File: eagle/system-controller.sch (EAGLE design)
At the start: 225 parts, among them J1 1, Q1 MOSFET-P-N-PAIR, Q10 MOSFET-P-N-PAIR, Q11 DNP/NTR4101P, Q2 MOSFET-P-N-PAIR, Q3 DON3035L, Q4 MOSFET-P-N-PAIR, Q5 MOSFET-P-N-PAIR, Q6 MOSFET-P-N-PAIR, Q7 MOSFET-P-N-PAIR, Q8 MOSFET-P-N-PAIR, Q9 DNP/NTR4101P, U1 TPS25944LRVCRWQFN-20-3X4, U10 TPS25944LRVCRWQFN-20-3X4, U11 ACPL-M61L, U12 ACPL-M61L, U13 TPS25944LRVCRWQFN-20-3X4, U14 ACPL-M61L, U15 ACPL-M61L, U2 LP5907MFX-3.0, U3 TPS25944LRVCRWQFN-20-3X4, U4 TPS25944LRVCRWQFN-20-3X4, U5 TPS25944LRVCRWQFN-20-3X4, U6 TPS25944LRVCRWQFN-20-3X4, U7 ATMEGA128L-8A(U/N), U8 TS4100, U9 TPS25944LRVCRWQFN-20-3X4, X1 8 MHz CRYSTAL-ABRACON-ABM3-SMD

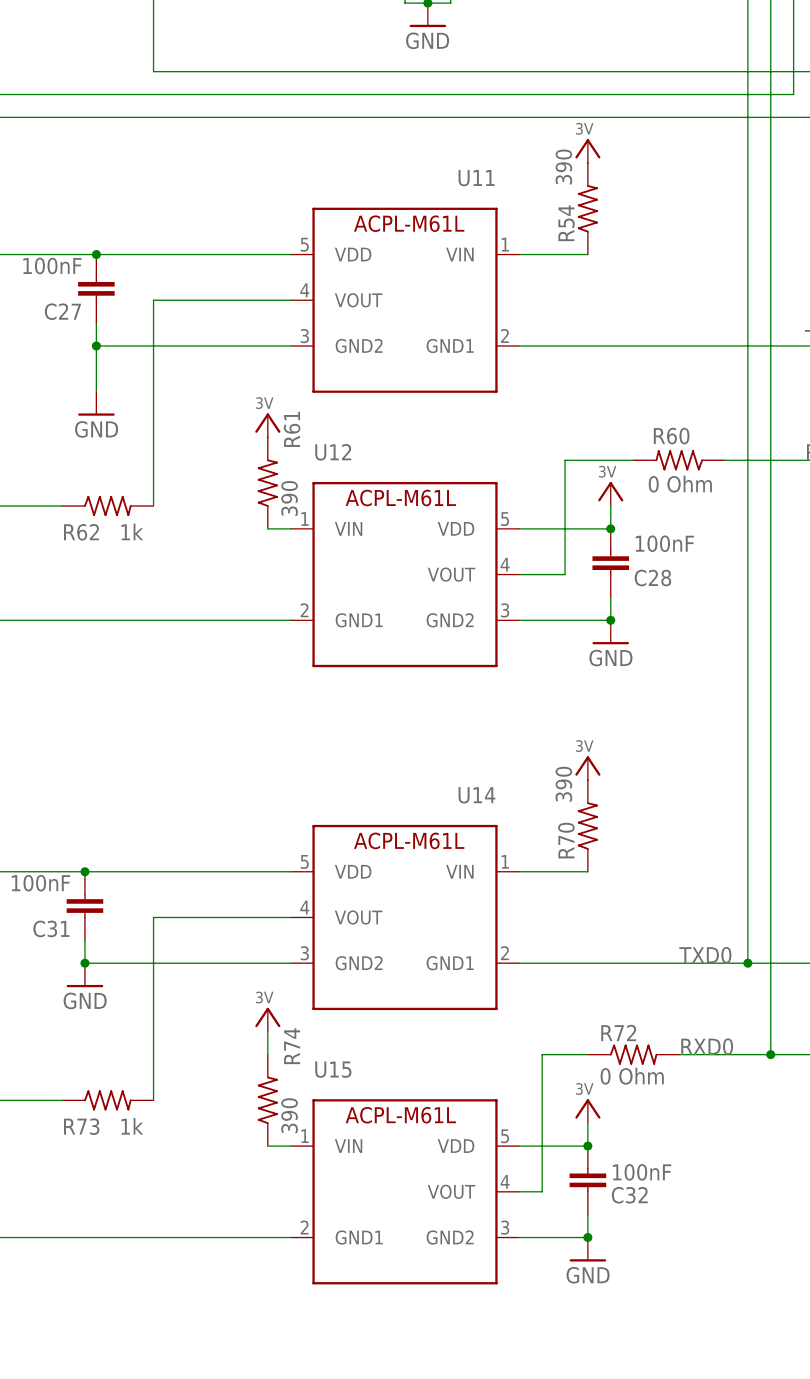
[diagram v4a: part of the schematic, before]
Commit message: Fixed opto-isolator symbol with proper labels
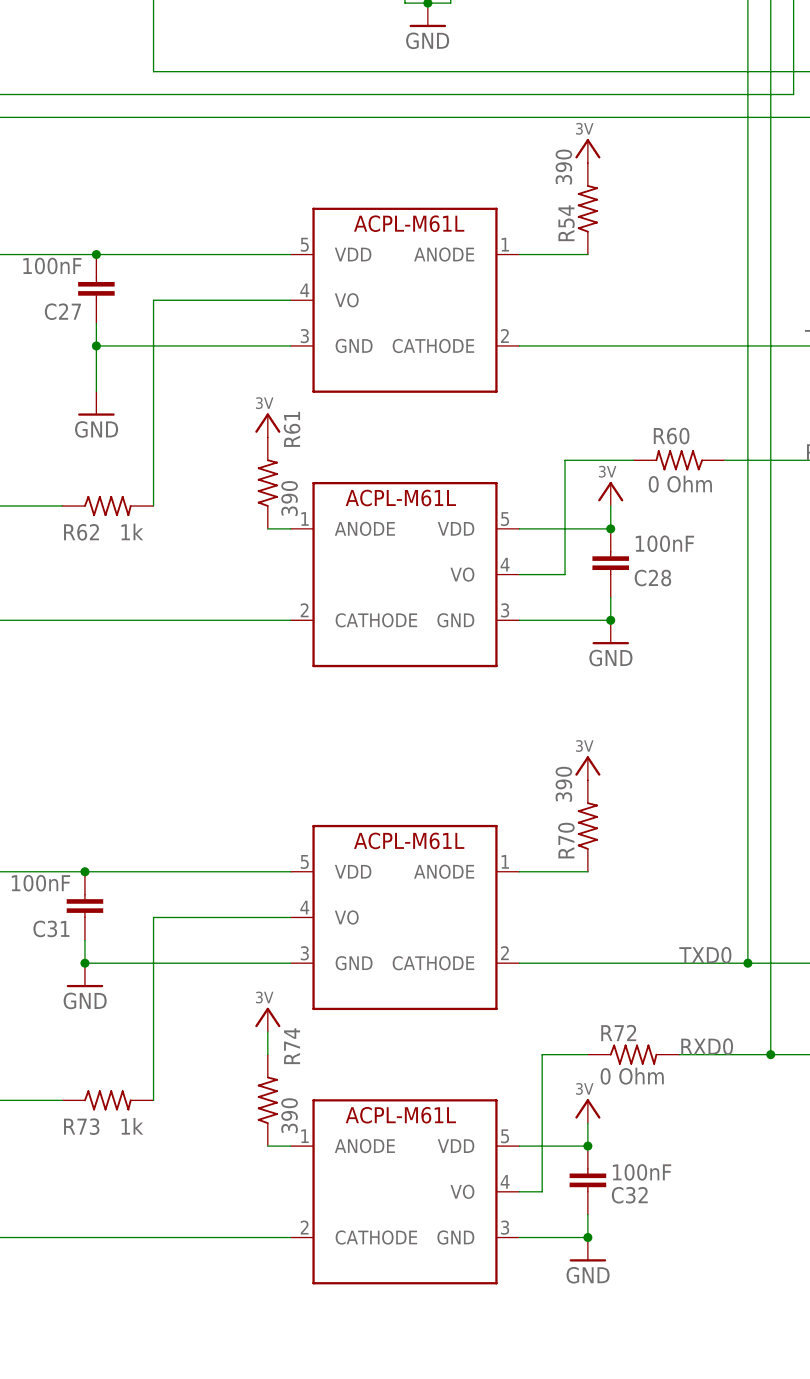
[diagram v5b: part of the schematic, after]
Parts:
- removed U11, U12, U14, U15: ACPL-M61L, v2_sync_box:ACPL-M61L
- added U$1, U$2, U$3, U$4: ACPL-M61L, system-controller:ACPL-M61L
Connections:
- net 3V: now also U$3.VDD, U$4.VDD; no longer U12.VDD, U15.VDD
- net GND: now also U$1.GND, U$2.GND, U$3.GND, U$4.GND; no longer U11.GND2, U12.GND2, U14.GND2, U15.GND2
- net N$16: now also U$2.VO; no longer U14.VOUT
- net N$18: now also U$4.VO; no longer U15.VOUT
- net N$24: now also U$3.VO; no longer U12.VOUT
- net N$4: now also U$2.ANODE; no longer U14.VIN
- net N$5: now also U$1.VO; no longer U11.VOUT
- net N$54: now also U$4.ANODE; no longer U15.VIN
- net N$58: now also U$1.ANODE; no longer U11.VIN
- net N$8: now also U$3.ANODE; no longer U12.VIN
- net TXD0: now also U$2.CATHODE; no longer U14.GND1
- net TXD1: now also U$1.CATHODE; no longer U11.GND1
- net UART_FC_TX: now also U$3.CATHODE; no longer U12.GND1
- net UART_FC_VCC: now also U$1.VDD; no longer U11.VDD
- net UART_LGR_TX: now also U$4.CATHODE; no longer U15.GND1
- net UART_LGR_VCC: now also U$2.VDD; no longer U14.VDD
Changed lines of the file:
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@@
 <?xml version="1.0" encoding="utf-8"?>
 <!DOCTYPE eagle SYSTEM "eagle.dtd">
-<eagle version="7.3.0">
+<eagle version="7.6.0">
 <drawing>
 <settings>
@@
 <attribute name="MPN" value="LP5907MFX-3.0/NOPB"/>
 </part>
-<part name="U11" library="v2_sync_box" deviceset="ACPL-M61L" device="">
-<attribute name="DIST" value="digikey"/>
-<attribute name="DPN" value="516-2169-5-ND"/>
-<attribute name="MFN" value="Broadcom"/>
-<attribute name="MPN" value="ACPL-M61L-000E"/>
-</part>
-<part name="U12" library="v2_sync_box" deviceset="ACPL-M61L" device="">
-<attribute name="DIST" value="digikey"/>
-<attribute name="DPN" value="516-2169-5-ND"/>
-<attribute name="MFN" value="Broadcom"/>
-<attribute name="MPN" value="ACPL-M61L-000E"/>
-</part>
-<part name="U14" library="v2_sync_box" deviceset="ACPL-M61L" device="">
-<attribute name="DIST" value="digikey"/>
-<attribute name="DPN" value="516-2169-5-ND"/>
-<attribute name="MFN" value="Broadcom"/>
-<attribute name="MPN" value="ACPL-M61L-000E"/>
-</part>
-<part name="U15" library="v2_sync_box" deviceset="ACPL-M61L" device="">
-<attribute name="DIST" value="digikey"/>
-<attribute name="DPN" value="516-2169-5-ND"/>
-<attribute name="MFN" value="Broadcom"/>
-<attribute name="MPN" value="ACPL-M61L-000E"/>
-</part>
 <part name="U1" library="system-controller" deviceset="TPS25944LRVCR" device="WQFN-20-3X4">
 <attribute name="DIST" value="digikey"/>
@@
 <part name="GND2" library="psas_c3_team05" deviceset="GND" device=""/>
 <part name="3V-11" library="supply-3v" deviceset="3V" device=""/>
+<part name="U$1" library="system-controller" deviceset="ACPL-M61L" device=""/>
+<part name="U$2" library="system-controller" deviceset="ACPL-M61L" device=""/>
+<part name="U$3" library="system-controller" deviceset="ACPL-M61L" device=""/>
+<part name="U$4" library="system-controller" deviceset="ACPL-M61L" device=""/>
 </parts>
 <sheets>
@@
 <attribute name="MPN" x="167.64" y="387.35" size="1.778" layer="96" display="off"/>
 </instance>
-<instance part="U11" gate="G$1" x="175.26" y="119.38" rot="MR0">
-<attribute name="DIST" x="175.26" y="119.38" size="1.778" layer="96" rot="MR0" display="off"/>
-<attribute name="DPN" x="175.26" y="119.38" size="1.778" layer="96" rot="MR0" display="off"/>
-<attribute name="MFN" x="175.26" y="119.38" size="1.778" layer="96" rot="MR0" display="off"/>
-<attribute name="MPN" x="175.26" y="119.38" size="1.778" layer="96" rot="MR0" display="off"/>
-</instance>
-<instance part="U12" gate="G$1" x="175.26" y="88.9">
-<attribute name="DIST" x="175.26" y="88.9" size="1.778" layer="96" display="off"/>
-<attribute name="MPN" x="175.26" y="88.9" size="1.778" layer="96" display="off"/>
-<attribute name="MFN" x="175.26" y="88.9" size="1.778" layer="96" display="off"/>
-<attribute name="DPN" x="175.26" y="88.9" size="1.778" layer="96" display="off"/>
-</instance>
-<instance part="U14" gate="G$1" x="175.26" y="50.8" rot="MR0">
-<attribute name="DIST" x="175.26" y="50.8" size="1.778" layer="96" rot="MR0" display="off"/>
-<attribute name="MPN" x="175.26" y="50.8" size="1.778" layer="96" rot="MR0" display="off"/>
-<attribute name="MFN" x="175.26" y="50.8" size="1.778" layer="96" rot="MR0" display="off"/>
-<attribute name="DPN" x="175.26" y="50.8" size="1.778" layer="96" rot="MR0" display="off"/>
-</instance>
-<instance part="U15" gate="G$1" x="175.26" y="20.32">
-<attribute name="DIST" x="175.26" y="20.32" size="1.778" layer="96" display="off"/>
-<attribute name="MPN" x="175.26" y="20.32" size="1.778" layer="96" display="off"/>
-<attribute name="MFN" x="175.26" y="20.32" size="1.778" layer="96" display="off"/>
-<attribute name="DPN" x="175.26" y="20.32" size="1.778" layer="96" display="off"/>
-</instance>
 <instance part="U1" gate="G$1" x="434.34" y="408.94">
 <attribute name="MPN" x="434.34" y="408.94" size="1.778" layer="96" display="off"/>
@@
 <instance part="GND2" gate="1" x="210.82" y="370.84"/>
 <instance part="3V-11" gate="G$1" x="210.82" y="393.7"/>
+<instance part="U$1" gate="G$1" x="175.26" y="119.38" rot="MR0"/>
+<instance part="U$2" gate="G$1" x="175.26" y="50.8" rot="MR0"/>
+<instance part="U$3" gate="G$1" x="175.26" y="88.9"/>
+<instance part="U$4" gate="G$1" x="175.26" y="20.32"/>
 </instances>
 <busses>
@@
 <segment>
 <wire x1="109.22" y1="83.82" x2="162.56" y2="83.82" width="0.1524" layer="91"/>
-<pinref part="U12" gate="G$1" pin="GND1"/>
 <label x="111.76" y="83.82" size="1.778" layer="95"/>
+<pinref part="U$3" gate="G$1" pin="CATHODE"/>
 </segment>
 </net>
@@
 <pinref part="LED11" gate="LED" pin="K"/>
 <wire x1="228.6" y1="45.72" x2="228.6" y2="48.26" width="0.1524" layer="91"/>
-<pinref part="U14" gate="G$1" pin="GND1"/>
+<pinref part="U$2" gate="G$1" pin="CATHODE"/>
 </segment>
 </net>
@@
 <wire x1="256.54" y1="114.3" x2="256.54" y2="121.92" width="0.1524" layer="91"/>
 <junction x="228.6" y="114.3"/>
-<pinref part="U11" gate="G$1" pin="GND1"/>
+<pinref part="U$1" gate="G$1" pin="CATHODE"/>
 </segment>
 </net>
@@
 <wire x1="147.32" y1="119.38" x2="147.32" y2="96.52" width="0.1524" layer="91"/>
 <pinref part="R62" gate="R" pin="2"/>
-<pinref part="U11" gate="G$1" pin="VOUT"/>
+<pinref part="U$1" gate="G$1" pin="VO"/>
 </segment>
 </net>
@@
 <wire x1="147.32" y1="50.8" x2="147.32" y2="30.48" width="0.1524" layer="91"/>
 <pinref part="R73" gate="R" pin="2"/>
-<pinref part="U14" gate="G$1" pin="VOUT"/>
+<pinref part="U$2" gate="G$1" pin="VO"/>
 </segment>
 </net>
@@
 <wire x1="187.96" y1="20.32" x2="190.5" y2="20.32" width="0.1524" layer="91"/>
 <wire x1="190.5" y1="20.32" x2="190.5" y2="35.56" width="0.1524" layer="91"/>
-<pinref part="U15" gate="G$1" pin="VOUT"/>
+<pinref part="U$4" gate="G$1" pin="VO"/>
 </segment>
 </net>
@@
 <segment>
 <wire x1="106.68" y1="15.24" x2="162.56" y2="15.24" width="0.1524" layer="91"/>
-<pinref part="U15" gate="G$1" pin="GND1"/>
 <label x="109.22" y="15.24" size="1.778" layer="95"/>
+<pinref part="U$4" gate="G$1" pin="CATHODE"/>
 </segment>
 </net>
@@
 <wire x1="193.04" y1="88.9" x2="187.96" y2="88.9" width="0.1524" layer="91"/>
 <pinref part="R60" gate="R" pin="2"/>
-<pinref part="U12" gate="G$1" pin="VOUT"/>
+<pinref part="U$3" gate="G$1" pin="VO"/>
 </segment>
 </net>
@@
 <pinref part="C31" gate="CE" pin="2"/>
 <junction x="139.7" y="55.88"/>
-<pinref part="U14" gate="G$1" pin="VDD"/>
+<pinref part="U$2" gate="G$1" pin="VDD"/>
 </segment>
 <segment>
@@
 <pinref part="C27" gate="CE" pin="2"/>
 <junction x="140.97" y="124.46"/>
-<pinref part="U11" gate="G$1" pin="VDD"/>
+<pinref part="U$1" gate="G$1" pin="VDD"/>
 </segment>
 <segment>
@@
 <wire x1="187.96" y1="93.98" x2="198.12" y2="93.98" width="0.1524" layer="91"/>
 <junction x="198.12" y="93.98"/>
-<pinref part="U12" gate="G$1" pin="VDD"/>
+<pinref part="U$3" gate="G$1" pin="VDD"/>
 </segment>
 <segment>
@@
 <junction x="195.58" y="25.4"/>
 <wire x1="187.96" y1="25.4" x2="195.58" y2="25.4" width="0.1524" layer="91"/>
-<pinref part="U15" gate="G$1" pin="VDD"/>
+<pinref part="U$4" gate="G$1" pin="VDD"/>
 </segment>
 <segment>
@@
 <pinref part="C28" gate="CE" pin="1"/>
 <wire x1="187.96" y1="83.82" x2="198.12" y2="83.82" width="0.1524" layer="91"/>
-<pinref part="U12" gate="G$1" pin="GND2"/>
+<pinref part="U$3" gate="G$1" pin="GND"/>
 </segment>
 <segment>
@@
 <junction x="140.97" y="114.3"/>
 <pinref part="C27" gate="CE" pin="1"/>
-<pinref part="U11" gate="G$1" pin="GND2"/>
+<pinref part="U$1" gate="G$1" pin="GND"/>
 </segment>
 <segment>
@@
 <junction x="139.7" y="45.72"/>
 <pinref part="C31" gate="CE" pin="1"/>
-<pinref part="U14" gate="G$1" pin="GND2"/>
+<pinref part="U$2" gate="G$1" pin="GND"/>
 </segment>
 <segment>
@@
 <pinref part="C32" gate="CE" pin="1"/>
 <wire x1="187.96" y1="15.24" x2="195.58" y2="15.24" width="0.1524" layer="91"/>
-<pinref part="U15" gate="G$1" pin="GND2"/>
+<pinref part="U$4" gate="G$1" pin="GND"/>
 </segment>
 <segment>
@@
 <wire x1="187.96" y1="124.46" x2="195.58" y2="124.46" width="0.1524" layer="91"/>
 <pinref part="R54" gate="R" pin="1"/>
-<pinref part="U11" gate="G$1" pin="VIN"/>
+<pinref part="U$1" gate="G$1" pin="ANODE"/>
 </segment>
 </net>
@@
 <pinref part="R70" gate="R" pin="1"/>
 <wire x1="187.96" y1="55.88" x2="195.58" y2="55.88" width="0.1524" layer="91"/>
-<pinref part="U14" gate="G$1" pin="VIN"/>
+<pinref part="U$2" gate="G$1" pin="ANODE"/>
 </segment>
 </net>
@@
 <pinref part="R61" gate="R" pin="1"/>
 <wire x1="160.02" y1="93.98" x2="162.56" y2="93.98" width="0.1524" layer="91"/>
-<pinref part="U12" gate="G$1" pin="VIN"/>
+<pinref part="U$3" gate="G$1" pin="ANODE"/>
 </segment>
 </net>
@@
 <pinref part="R74" gate="R" pin="1"/>
 <wire x1="162.56" y1="25.4" x2="160.02" y2="25.4" width="0.1524" layer="91"/>
-<pinref part="U15" gate="G$1" pin="VIN"/>
+<pinref part="U$4" gate="G$1" pin="ANODE"/>
 </segment>
 </net>
